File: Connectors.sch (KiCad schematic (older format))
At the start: 4 parts

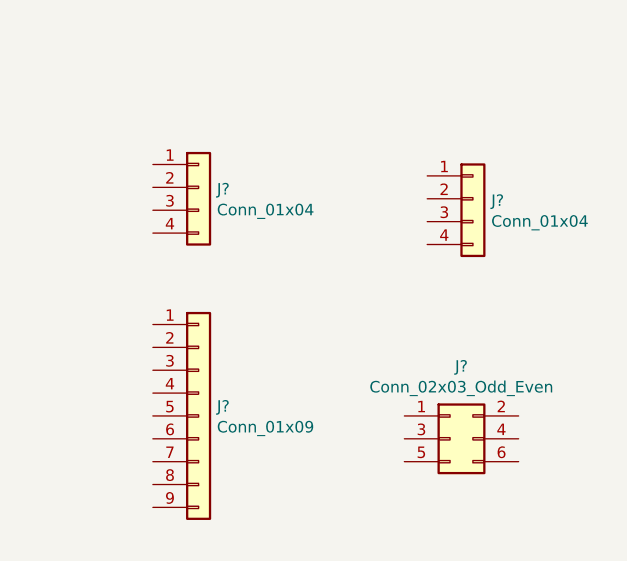
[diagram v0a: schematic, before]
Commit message: Addded footprints
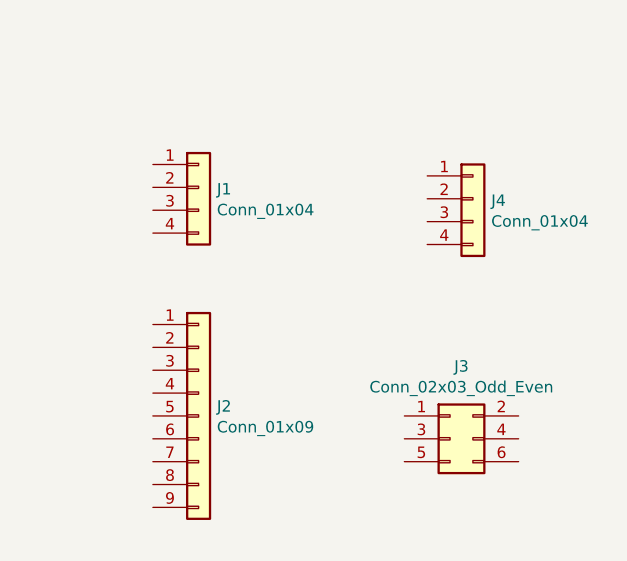
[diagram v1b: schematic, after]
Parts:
- J1, J4: renamed from J?; footprint (none) -> Connector_PinSocket_2.54mm:PinSocket_1x04_P2.54mm_Vertical
- J2: renamed from J?; footprint (none) -> Connector_PinSocket_2.54mm:PinSocket_1x09_P2.54mm_Vertical
- J3: renamed from J?; footprint (none) -> Connector_PinSocket_2.54mm:PinSocket_2x03_P2.54mm_Vertical
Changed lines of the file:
@@
 $EndDescr
 $Comp
-L Connector_Generic:Conn_01x09 J?
+L Connector_Generic:Conn_01x09 J2
 U 1 1 5EC184F5
 P 5100 4350
-F 0 "J?" H 5180 4392 50  0000 L CNN
+F 0 "J2" H 5180 4392 50  0000 L CNN
 F 1 "Conn_01x09" H 5180 4301 50  0000 L CNN
-F 2 "" H 5100 4350 50  0001 C CNN
+F 2 "Connector_PinSocket_2.54mm:PinSocket_1x09_P2.54mm_Vertical" H 5100 4350 50  0001 C CNN
 F 3 "~" H 5100 4350 50  0001 C CNN
 	1    5100 4350
@@
 $EndComp
 $Comp
-L Connector_Generic:Conn_01x04 J?
+L Connector_Generic:Conn_01x04 J4
 U 1 1 5EC18C97
 P 6300 3400
-F 0 "J?" H 6380 3392 50  0000 L CNN
+F 0 "J4" H 6380 3392 50  0000 L CNN
 F 1 "Conn_01x04" H 6380 3301 50  0000 L CNN
-F 2 "" H 6300 3400 50  0001 C CNN
+F 2 "Connector_PinSocket_2.54mm:PinSocket_1x04_P2.54mm_Vertical" H 6300 3400 50  0001 C CNN
 F 3 "~" H 6300 3400 50  0001 C CNN
 	1    6300 3400
@@
 $EndComp
 $Comp
-L Connector_Generic:Conn_02x03_Odd_Even J?
+L Connector_Generic:Conn_02x03_Odd_Even J3
 U 1 1 5EC194FF
 P 6200 4450
-F 0 "J?" H 6250 4767 50  0000 C CNN
+F 0 "J3" H 6250 4767 50  0000 C CNN
 F 1 "Conn_02x03_Odd_Even" H 6250 4676 50  0000 C CNN
-F 2 "" H 6200 4450 50  0001 C CNN
+F 2 "Connector_PinSocket_2.54mm:PinSocket_2x03_P2.54mm_Vertical" H 6200 4450 50  0001 C CNN
 F 3 "~" H 6200 4450 50  0001 C CNN
 	1    6200 4450
@@
 $EndComp
 $Comp
-L Connector_Generic:Conn_01x04 J?
+L Connector_Generic:Conn_01x04 J1
 U 1 1 5EC1A01F
 P 5100 3350
-F 0 "J?" H 5180 3342 50  0000 L CNN
+F 0 "J1" H 5180 3342 50  0000 L CNN
 F 1 "Conn_01x04" H 5180 3251 50  0000 L CNN
-F 2 "" H 5100 3350 50  0001 C CNN
+F 2 "Connector_PinSocket_2.54mm:PinSocket_1x04_P2.54mm_Vertical" H 5100 3350 50  0001 C CNN
 F 3 "~" H 5100 3350 50  0001 C CNN
 	1    5100 3350

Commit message: Completed wiring in connector sheet
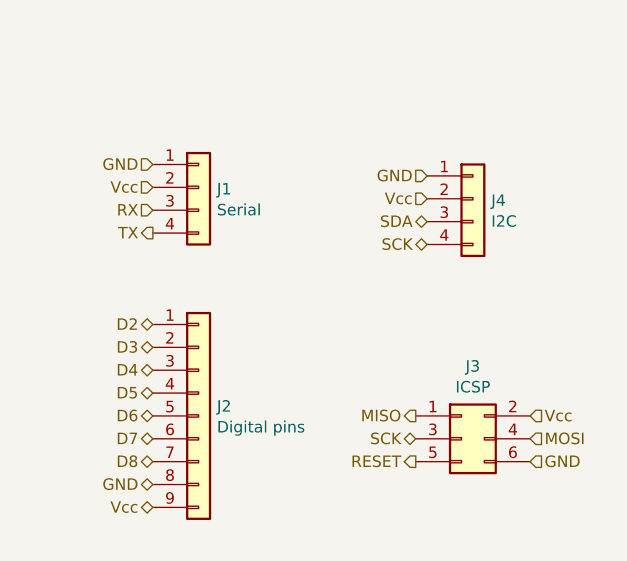
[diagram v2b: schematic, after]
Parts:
- J1: value Conn_01x04 -> Serial
- J2: value Conn_01x09 -> Digital pins
- J3: value Conn_02x03_Odd_Even -> ICSP
- J4: value Conn_01x04 -> I2C
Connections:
- net D2: now reaches J2.1 (Pin_1)
- net D3: now reaches J2.2 (Pin_2)
- net D4: now reaches J2.3 (Pin_3)
- net D5: now reaches J2.4 (Pin_4)
- net D6: now reaches J2.5 (Pin_5)
- net D7: now reaches J2.6 (Pin_6)
- net D8: now reaches J2.7 (Pin_7)
- net GND: now reaches J2.8 (Pin_8)
- net GND: now also J1.1 (Pin_1), J3.6 (Pin_6), J4.1 (Pin_1)
- net Vcc: now reaches J2.9 (Pin_9)
- net Vcc: now also J1.2 (Pin_2), J3.2 (Pin_2), J4.2 (Pin_2)
- net SDA: now reaches J4.3 (Pin_3)
- net SCK: now reaches J4.4 (Pin_4)
- net SCK: now also J3.3 (Pin_3)
- net MISO: now reaches J3.1 (Pin_1)
- net MOSI: now reaches J3.4 (Pin_4)
- net RESET: now reaches J3.5 (Pin_5)
- net RX: now reaches J1.3 (Pin_3)
- net TX: now reaches J1.4 (Pin_4)
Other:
- moved on the sheet: J3
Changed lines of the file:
@@
 P 5100 4350
 F 0 "J2" H 5180 4392 50  0000 L CNN
-F 1 "Conn_01x09" H 5180 4301 50  0000 L CNN
+F 1 "Digital pins" H 5180 4301 50  0000 L CNN
 F 2 "Connector_PinSocket_2.54mm:PinSocket_1x09_P2.54mm_Vertical" H 5100 4350 50  0001 C CNN
 F 3 "~" H 5100 4350 50  0001 C CNN
@@
 P 6300 3400
 F 0 "J4" H 6380 3392 50  0000 L CNN
-F 1 "Conn_01x04" H 6380 3301 50  0000 L CNN
+F 1 "I2C" H 6380 3301 50  0000 L CNN
 F 2 "Connector_PinSocket_2.54mm:PinSocket_1x04_P2.54mm_Vertical" H 6300 3400 50  0001 C CNN
 F 3 "~" H 6300 3400 50  0001 C CNN
@@
 L Connector_Generic:Conn_02x03_Odd_Even J3
 U 1 1 5EC194FF
-P 6200 4450
-F 0 "J3" H 6250 4767 50  0000 C CNN
-F 1 "Conn_02x03_Odd_Even" H 6250 4676 50  0000 C CNN
-F 2 "Connector_PinSocket_2.54mm:PinSocket_2x03_P2.54mm_Vertical" H 6200 4450 50  0001 C CNN
-F 3 "~" H 6200 4450 50  0001 C CNN
-	1    6200 4450
+P 6250 4450
+F 0 "J3" H 6300 4767 50  0000 C CNN
+F 1 "ICSP" H 6300 4676 50  0000 C CNN
+F 2 "Connector_PinSocket_2.54mm:PinSocket_2x03_P2.54mm_Vertical" H 6250 4450 50  0001 C CNN
+F 3 "~" H 6250 4450 50  0001 C CNN
+	1    6250 4450
 	1    0    0    -1
 $EndComp
@@
 P 5100 3350
 F 0 "J1" H 5180 3342 50  0000 L CNN
-F 1 "Conn_01x04" H 5180 3251 50  0000 L CNN
+F 1 "Serial" H 5180 3251 50  0000 L CNN
 F 2 "Connector_PinSocket_2.54mm:PinSocket_1x04_P2.54mm_Vertical" H 5100 3350 50  0001 C CNN
 F 3 "~" H 5100 3350 50  0001 C CNN
@@
 	1    0    0    -1
 $EndComp
+Text HLabel 6050 4350 0    50   Output ~ 0
+MISO
+Text HLabel 6050 4450 0    50   BiDi ~ 0
+SCK
+Text HLabel 6050 4550 0    50   Output ~ 0
+RESET
+Text HLabel 6550 4350 2    50   Input ~ 0
+Vcc
+Text HLabel 6550 4450 2    50   Input ~ 0
+MOSI
+Text HLabel 6550 4550 2    50   Input ~ 0
+GND
+Text HLabel 4900 3250 0    50   Input ~ 0
+GND
+Text HLabel 4900 3350 0    50   Input ~ 0
+Vcc
+Text HLabel 4900 3450 0    50   Input ~ 0
+RX
+Text HLabel 4900 3550 0    50   Output ~ 0
+TX
+Text HLabel 6100 3300 0    50   Input ~ 0
+GND
+Text HLabel 6100 3400 0    50   Input ~ 0
+Vcc
+Text HLabel 6100 3500 0    50   BiDi ~ 0
+SDA
+Text HLabel 6100 3600 0    50   BiDi ~ 0
+SCK
+Text HLabel 4900 3950 0    50   BiDi ~ 0
+D2
+Text HLabel 4900 4050 0    50   BiDi ~ 0
+D3
+Text HLabel 4900 4150 0    50   BiDi ~ 0
+D4
+Text HLabel 4900 4250 0    50   BiDi ~ 0
+D5
+Text HLabel 4900 4350 0    50   BiDi ~ 0
+D6
+Text HLabel 4900 4550 0    50   BiDi ~ 0
+D8
+Text HLabel 4900 4650 0    50   BiDi ~ 0
+GND
+Text HLabel 4900 4450 0    50   BiDi ~ 0
+D7
+Text HLabel 4900 4750 0    50   BiDi ~ 0
+Vcc
 $EndSCHEMATC

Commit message: Added functional block descriptions
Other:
- note added: "N5 - I2C Connector"
- note added: "N6 - Serial Connector"
- note added: "N7 - GPIO Connector"
- note added: "N8 - SPI Connector"
- moved on the sheet: J1, J2, J4
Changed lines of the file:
@@
 L Connector_Generic:Conn_01x09 J2
 U 1 1 5EC184F5
-P 5100 4350
-F 0 "J2" H 5180 4392 50  0000 L CNN
-F 1 "Digital pins" H 5180 4301 50  0000 L CNN
-F 2 "Connector_PinSocket_2.54mm:PinSocket_1x09_P2.54mm_Vertical" H 5100 4350 50  0001 C CNN
-F 3 "~" H 5100 4350 50  0001 C CNN
-	1    5100 4350
+P 5100 4450
+F 0 "J2" H 5180 4492 50  0000 L CNN
+F 1 "Digital pins" H 5180 4401 50  0000 L CNN
+F 2 "Connector_PinSocket_2.54mm:PinSocket_1x09_P2.54mm_Vertical" H 5100 4450 50  0001 C CNN
+F 3 "~" H 5100 4450 50  0001 C CNN
+	1    5100 4450
 	1    0    0    -1
 $EndComp
@@
 L Connector_Generic:Conn_01x04 J4
 U 1 1 5EC18C97
-P 6300 3400
-F 0 "J4" H 6380 3392 50  0000 L CNN
-F 1 "I2C" H 6380 3301 50  0000 L CNN
-F 2 "Connector_PinSocket_2.54mm:PinSocket_1x04_P2.54mm_Vertical" H 6300 3400 50  0001 C CNN
-F 3 "~" H 6300 3400 50  0001 C CNN
-	1    6300 3400
+P 6350 3050
+F 0 "J4" H 6430 3042 50  0000 L CNN
+F 1 "I2C" H 6430 2951 50  0000 L CNN
+F 2 "Connector_PinSocket_2.54mm:PinSocket_1x04_P2.54mm_Vertical" H 6350 3050 50  0001 C CNN
+F 3 "~" H 6350 3050 50  0001 C CNN
+	1    6350 3050
 	1    0    0    -1
 $EndComp
@@
 L Connector_Generic:Conn_01x04 J1
 U 1 1 5EC1A01F
-P 5100 3350
-F 0 "J1" H 5180 3342 50  0000 L CNN
-F 1 "Serial" H 5180 3251 50  0000 L CNN
-F 2 "Connector_PinSocket_2.54mm:PinSocket_1x04_P2.54mm_Vertical" H 5100 3350 50  0001 C CNN
-F 3 "~" H 5100 3350 50  0001 C CNN
-	1    5100 3350
+P 5100 3000
+F 0 "J1" H 5180 2992 50  0000 L CNN
+F 1 "Serial" H 5180 2901 50  0000 L CNN
+F 2 "Connector_PinSocket_2.54mm:PinSocket_1x04_P2.54mm_Vertical" H 5100 3000 50  0001 C CNN
+F 3 "~" H 5100 3000 50  0001 C CNN
+	1    5100 3000
 	1    0    0    -1
 $EndComp
@@
 Text HLabel 6550 4550 2    50   Input ~ 0
 GND
-Text HLabel 4900 3250 0    50   Input ~ 0
+Text HLabel 4900 2900 0    50   Input ~ 0
 GND
-Text HLabel 4900 3350 0    50   Input ~ 0
+Text HLabel 4900 3000 0    50   Input ~ 0
 Vcc
-Text HLabel 4900 3450 0    50   Input ~ 0
+Text HLabel 4900 3100 0    50   Input ~ 0
 RX
-Text HLabel 4900 3550 0    50   Output ~ 0
+Text HLabel 4900 3200 0    50   Output ~ 0
 TX
-Text HLabel 6100 3300 0    50   Input ~ 0
+Text HLabel 6150 2950 0    50   Input ~ 0
 GND
-Text HLabel 6100 3400 0    50   Input ~ 0
+Text HLabel 6150 3050 0    50   Input ~ 0
 Vcc
-Text HLabel 6100 3500 0    50   BiDi ~ 0
+Text HLabel 6150 3150 0    50   BiDi ~ 0
 SDA
-Text HLabel 6100 3600 0    50   BiDi ~ 0
+Text HLabel 6150 3250 0    50   BiDi ~ 0
 SCK
-Text HLabel 4900 3950 0    50   BiDi ~ 0
+Text HLabel 4900 4050 0    50   BiDi ~ 0
 D2
-Text HLabel 4900 4050 0    50   BiDi ~ 0
+Text HLabel 4900 4150 0    50   BiDi ~ 0
 D3
-Text HLabel 4900 4150 0    50   BiDi ~ 0
+Text HLabel 4900 4250 0    50   BiDi ~ 0
 D4
-Text HLabel 4900 4250 0    50   BiDi ~ 0
+Text HLabel 4900 4350 0    50   BiDi ~ 0
 D5
-Text HLabel 4900 4350 0    50   BiDi ~ 0
+Text HLabel 4900 4450 0    50   BiDi ~ 0
 D6
+Text HLabel 4900 4650 0    50   BiDi ~ 0
+D8
+Text HLabel 4900 4750 0    50   BiDi ~ 0
+GND
 Text HLabel 4900 4550 0    50   BiDi ~ 0
-D8
-Text HLabel 4900 4650 0    50   BiDi ~ 0
-GND
-Text HLabel 4900 4450 0    50   BiDi ~ 0
 D7
-Text HLabel 4900 4750 0    50   BiDi ~ 0
+Text HLabel 4900 4850 0    50   BiDi ~ 0
 Vcc
+Text Notes 5350 2700 2    50   ~ 0
+N6 - Serial Connector
+Text Notes 6500 2700 2    50   ~ 0
+N5 - I2C Connector
+Text Notes 5350 3900 2    50   ~ 0
+N7 - GPIO Connector
+Text Notes 6700 4050 2    50   ~ 0
+N8 - SPI Connector
 $EndSCHEMATC
